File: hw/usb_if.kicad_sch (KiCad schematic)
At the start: 13 parts, among them J1 USB_C_Receptacle_USB2.0, U16 USB3343

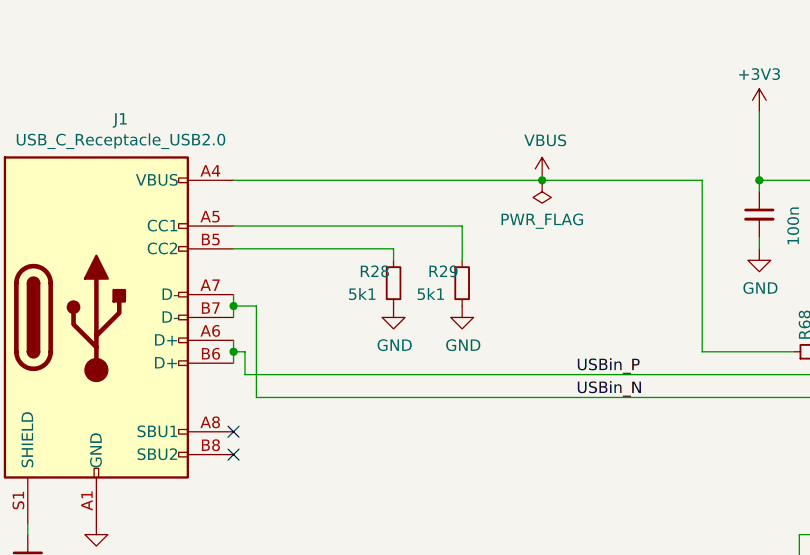
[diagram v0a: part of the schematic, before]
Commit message: renaming, comments, part/vendor and other cosmetics (no pcb change)
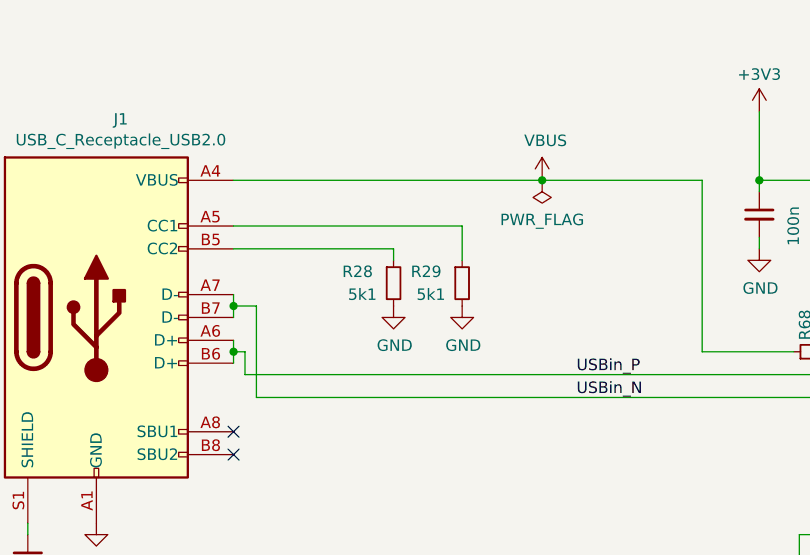
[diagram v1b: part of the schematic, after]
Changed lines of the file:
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@@
   (symbol (lib_id "Device:R_Small") (at 86.36 69.85 0) (unit 1)
     (in_bom yes) (on_board yes) (dnp no)
-    (property "Reference" "R28" (at 82.55 68.58 0)
+    (property "Reference" "R28" (at 80.645 68.58 0)
       (effects (font (size 1.27 1.27)) (justify left))
     )
@@
   (symbol (lib_id "Device:R_Small") (at 93.98 69.85 0) (unit 1)
     (in_bom yes) (on_board yes) (dnp no)
-    (property "Reference" "R29" (at 90.17 68.58 0)
+    (property "Reference" "R29" (at 88.265 68.58 0)
       (effects (font (size 1.27 1.27)) (justify left))
     )

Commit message: updated parts assignments
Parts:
- C100, C91: Manufacturer (none) -> Samsung; Part (none) -> CL10B104KB8NFNC
- R12: Manufacturer (none) -> Stackpole; Part (none) -> RMCF0603ZT0R00
- R16, R68: Manufacturer (none) -> Stackpole; Part (none) -> RMCF0603FT10K0
- R28, R29: Manufacturer (none) -> Stackpole; Part (none) -> RMCF0603FT5K10
- R67: Manufacturer (none) -> Stackpole; Part (none) -> RMCF0603FT8K06
- U16: Manufacturer (none) -> MicroChip; Part (none) -> USB3343-CP-TR
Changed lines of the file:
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@@
+			)
+		)
+		(property "Manufacturer" "Samsung"
+			(at 160.02 46.99 0)
+			(effects
+				(font
+					(size 1.27 1.27)
+				)
+				(hide yes)
+			)
+		)
+		(property "Part" "CL10B104KB8NFNC"
+			(at 160.02 46.99 0)
+			(effects
+				(font
+					(size 1.27 1.27)
+				)
+				(hide yes)
 			)
 		)
@@
 			)
 		)
+		(property "Manufacturer" "MicroChip"
+			(at 157.48 85.09 0)
+			(effects
+				(font
+					(size 1.27 1.27)
+				)
+				(hide yes)
+			)
+		)
+		(property "Part" "USB3343-CP-TR"
+			(at 157.48 85.09 0)
+			(effects
+				(font
+					(size 1.27 1.27)
+				)
+				(hide yes)
+			)
+		)
 		(pin "1"
 		)
@@
 			)
 		)
+		(property "Manufacturer" "Stackpole"
+			(at 86.36 69.85 0)
+			(effects
+				(font
+					(size 1.27 1.27)
+				)
+				(hide yes)
+			)
+		)
+		(property "Part" "RMCF0603FT5K10"
+			(at 86.36 69.85 0)
+			(effects
+				(font
+					(size 1.27 1.27)
+				)
+				(hide yes)
+			)
+		)
 		(pin "1"
 		)
@@
 		)
 		(property "Description" ""
+			(at 93.98 69.85 0)
+			(effects
+				(font
+					(size 1.27 1.27)
+				)
+				(hide yes)
+			)
+		)
+		(property "Manufacturer" "Stackpole"
+			(at 93.98 69.85 0)
+			(effects
+				(font
+					(size 1.27 1.27)
+				)
+				(hide yes)
+			)
+		)
+		(property "Part" "RMCF0603FT5K10"
 			(at 93.98 69.85 0)
 			(effects
@@
 			)
 		)
+		(property "Manufacturer" "Stackpole"
+			(at 142.24 109.22 0)
+			(effects
+				(font
+					(size 1.27 1.27)
+				)
+				(hide yes)
+			)
+		)
+		(property "Part" "RMCF0603FT8K06"
+			(at 142.24 109.22 0)
+			(effects
+				(font
+					(size 1.27 1.27)
+				)
+				(hide yes)
+			)
+		)
 		(pin "1"
 		)
@@
 			)
 		)
+		(property "Manufacturer" "Stackpole"
+			(at 133.35 77.47 0)
+			(effects
+				(font
+					(size 1.27 1.27)
+				)
+				(hide yes)
+			)
+		)
+		(property "Part" "RMCF0603FT10K0"
+			(at 133.35 77.47 0)
+			(effects
+				(font
+					(size 1.27 1.27)
+				)
+				(hide yes)
+			)
+		)
 		(pin "1"
 		)
@@
 			)
 		)
+		(property "Manufacturer" "Stackpole"
+			(at 175.895 57.15 0)
+			(effects
+				(font
+					(size 1.27 1.27)
+				)
+				(hide yes)
+			)
+		)
+		(property "Part" "RMCF0603FT10K0"
+			(at 175.895 57.15 0)
+			(effects
+				(font
+					(size 1.27 1.27)
+				)
+				(hide yes)
+			)
+		)
 		(pin "1"
 		)
@@
 			)
 		)
+		(property "Manufacturer" "Samsung"
+			(at 157.48 46.99 0)
+			(effects
+				(font
+					(size 1.27 1.27)
+				)
+				(hide yes)
+			)
+		)
+		(property "Part" "CL10B104KB8NFNC"
+			(at 157.48 46.99 0)
+			(effects
+				(font
+					(size 1.27 1.27)
+				)
+				(hide yes)
+			)
+		)
 		(pin "1"
 		)
@@
 			(at 187.325 60.325 0)
 			(effects
+				(font
+					(size 1.27 1.27)
+				)
+				(hide yes)
+			)
+		)
+		(property "Manufacturer" "Stackpole"
+			(at 187.325 60.325 0)
+			(effects
+				(font
+					(size 1.27 1.27)
+				)
+				(hide yes)
+			)
+		)
+		(property "Part" "  RMCF0603ZT0R00"
+			(at 187.325 60.325 0)
+			(effects

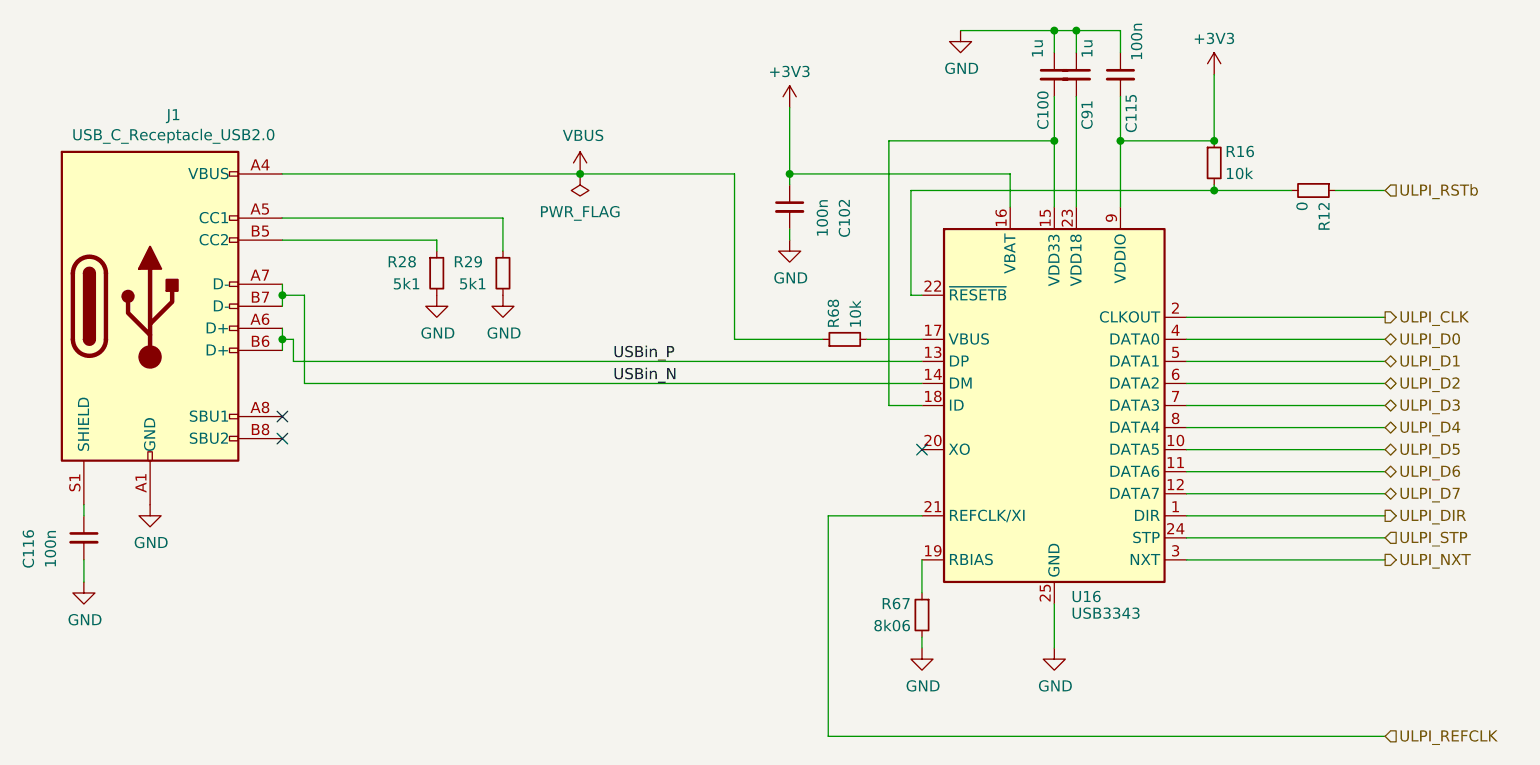
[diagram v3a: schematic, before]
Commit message: connected versaclock CLKSEL to ULPI RSTB (share FPGA pin)
ULPI Rstb is unlikely to be used

Also: - update of kicad to 9.0 (many library footprints updated)
      - added sheet titles, author
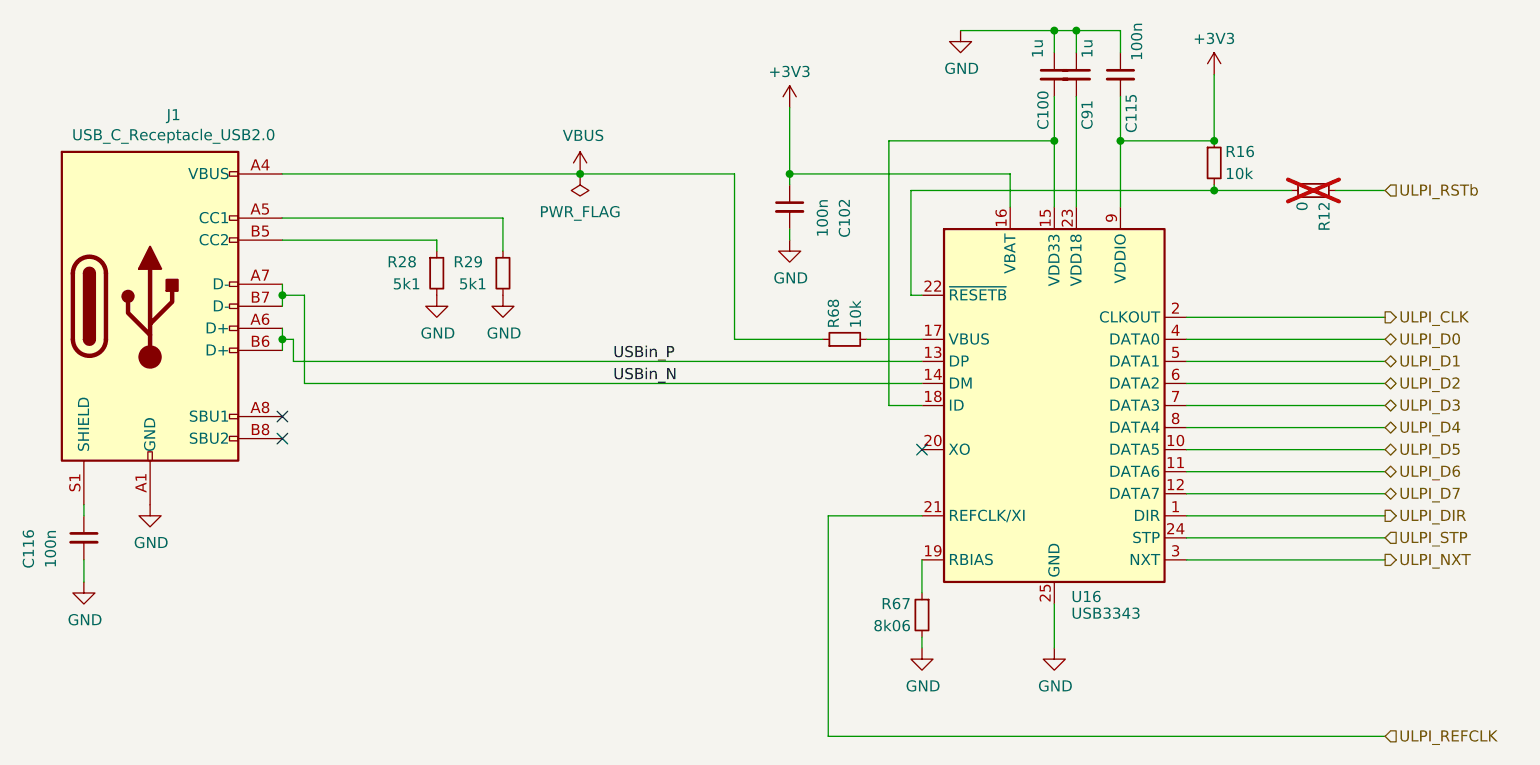
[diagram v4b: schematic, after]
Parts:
- R12: now not fitted; now left out of the parts list
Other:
- company: (none) -> Till Straumann
- title: (none) -> USB Phy
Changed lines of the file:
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@@
 (kicad_sch
-	(version 20231120)
+	(version 20250114)
 	(generator "eeschema")
-	(generator_version "8.0")
+	(generator_version "9.0")
 	(paper "A4")
+	(title_block
+		(title "USB Phy")
+		(rev "3.3b")
+		(company "Till Straumann")
+	)
 	(junction
 		(at 68.58 72.39)
@@
 		(unit 1)
 		(exclude_from_sim no)
-		(in_bom yes)
+		(in_bom no)
 		(on_board yes)
-		(dnp no)
+		(dnp yes)
 		(property "Reference" "R12"
 			(at 188.595 61.595 0)

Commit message: Added licensing information
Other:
- company: Till Straumann -> Copyright Till Straumann, 2025
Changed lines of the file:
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@@
 		(title "USB Phy")
 		(rev "3.3b")
-		(company "Till Straumann")
+		(company "Copyright Till Straumann, 2025")
+		(comment 1 "License: CERN-OHL-P v2")
 	)
 	(junction
